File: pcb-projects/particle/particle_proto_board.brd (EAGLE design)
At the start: 100 x 80 mm, 5 parts, among them IC1 ATTINY20-SOIC-14S1, IC2 DMC2400UV-SOT563, IC3 DMC2400UV-SOT563

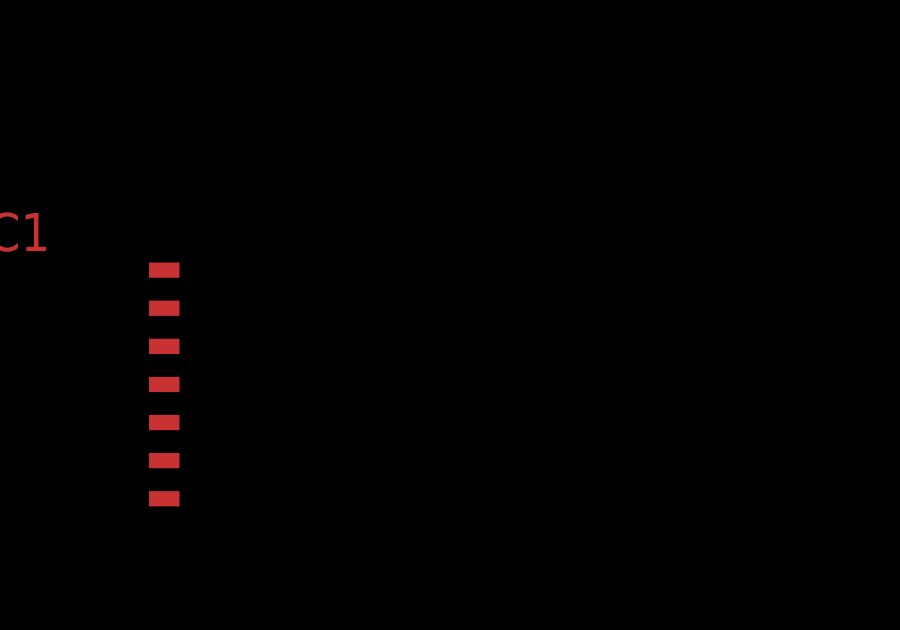
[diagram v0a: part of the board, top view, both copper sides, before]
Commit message: begun with tpi connector
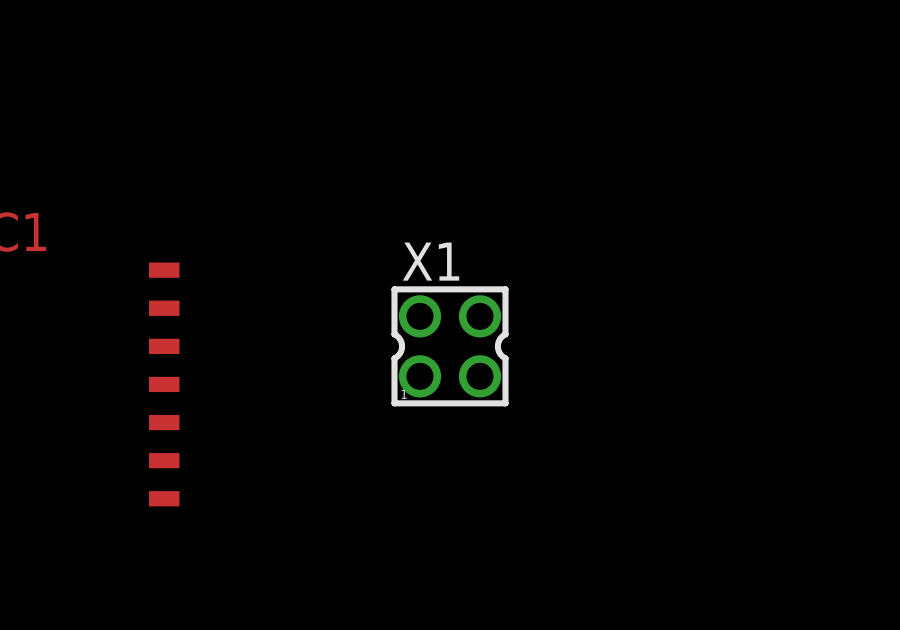
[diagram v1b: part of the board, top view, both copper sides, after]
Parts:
- added X1: 332-04, con-garry:332-04
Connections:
- net PWR_RX_B_SW renamed PWR_RX_SW_B
- new net N$4: IC1.11
- new net N$5: IC1.12
- new net N$6: IC1.13
- new net PWR_RX_SW_A: IC1.8, IC2.5
- new net RESET: IC1.3
- new net TPI_CLK: IC1.2
- net PWR_RX_A_SW: no longer IC2.5
- net PWR_TX_A: now also IC1.10; no longer IC1.2
- net RX_A: now also IC1.9; no longer IC1.3
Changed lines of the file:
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@@
 <?xml version="1.0" encoding="utf-8"?>
 <!DOCTYPE eagle SYSTEM "eagle.dtd">
-<eagle version="6.6.0">
+<eagle version="7.2.0">
 <drawing>
 <settings>
@@
 <pass name="Default">
 <param name="RoutingGrid" value="50mil"/>
+<param name="AutoGrid" value="1"/>
+<param name="Efforts" value="0"/>
+<param name="TopRouterVariant" value="1"/>
 <param name="tpViaShape" value="round"/>
 <param name="PrefDir.1" value="|"/>
@@
 <element name="R1" library="rcl" package="R1206" value="1k" x="27.94" y="34.29" rot="R180"/>
 <element name="R2" library="rcl" package="R1206" value="1k" x="27.94" y="26.67" rot="R180"/>
+<element name="X1" library="con-garry" package="332-04" value="332-04" x="60.96" y="30.48"/>
 </elements>
 <signals>
@@
 <wire x1="51.435" y1="33.02" x2="36.06" y2="32.32" width="0" layer="19" extent="1-1"/>
 </signal>
-<signal name="PWR_TX_A">
+<signal name="TPI_CLK">
 <contactref element="IC1" pad="2"/>
-<contactref element="IC2" pad="2"/>
-<wire x1="45.085" y1="31.75" x2="35.56" y2="33.72" width="0" layer="19" extent="1-1"/>
 </signal>
 <signal name="PWR_TX_B">
@@
 <wire x1="35.56" y1="27.37" x2="45.085" y2="27.94" width="0" layer="19" extent="1-1"/>
 </signal>
-<signal name="RX_A">
+<signal name="RESET">
 <contactref element="IC1" pad="3"/>
-<contactref element="IC2" pad="3"/>
-<wire x1="45.085" y1="30.48" x2="35.06" y2="33.72" width="0" layer="19" extent="1-1"/>
 </signal>
 <signal name="PWR_RX_A_SW">
 <contactref element="IC1" pad="4"/>
-<contactref element="IC2" pad="5"/>
-<wire x1="45.085" y1="29.21" x2="35.56" y2="32.32" width="0" layer="19" extent="1-1"/>
 </signal>
 <signal name="RX_B">
@@
 <wire x1="35.06" y1="27.37" x2="45.085" y2="26.67" width="0" layer="19" extent="1-1"/>
 </signal>
-<signal name="PWR_RX_B_SW">
+<signal name="PWR_RX_SW_B">
 <contactref element="IC1" pad="7"/>
 <contactref element="IC3" pad="5"/>
@@
 <wire x1="29.362" y1="26.67" x2="36.06" y2="27.37" width="0" layer="19" extent="1-1"/>
 </signal>
+<signal name="PWR_RX_SW_A">
+<contactref element="IC1" pad="8"/>
+<contactref element="IC2" pad="5"/>
+<wire x1="35.56" y1="32.32" x2="51.435" y2="25.4" width="0" layer="19" extent="1-1"/>
+</signal>
+<signal name="RX_A">
+<contactref element="IC1" pad="9"/>
+<contactref element="IC2" pad="3"/>
+<wire x1="35.06" y1="33.72" x2="51.435" y2="26.67" width="0" layer="19" extent="1-1"/>
+</signal>
+<signal name="PWR_TX_A">
+<contactref element="IC1" pad="10"/>
+<contactref element="IC2" pad="2"/>
+<wire x1="35.56" y1="33.72" x2="51.435" y2="27.94" width="0" layer="19" extent="1-1"/>
+</signal>
+<signal name="N$4">
+<contactref element="IC1" pad="11"/>
+</signal>
+<signal name="N$5">
+<contactref element="IC1" pad="12"/>
+</signal>
+<signal name="N$6">
+<contactref element="IC1" pad="13"/>
+</signal>
 </signals>

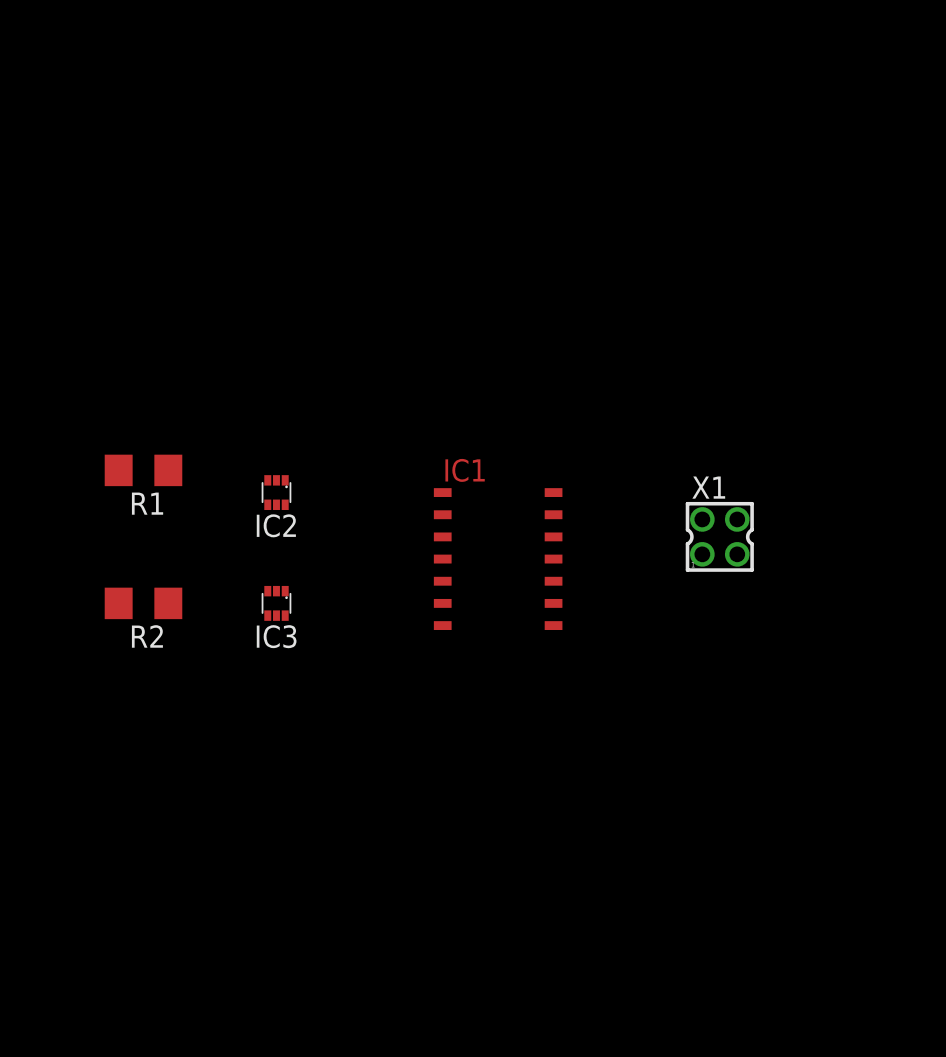
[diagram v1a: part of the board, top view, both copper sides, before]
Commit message: begun with routing
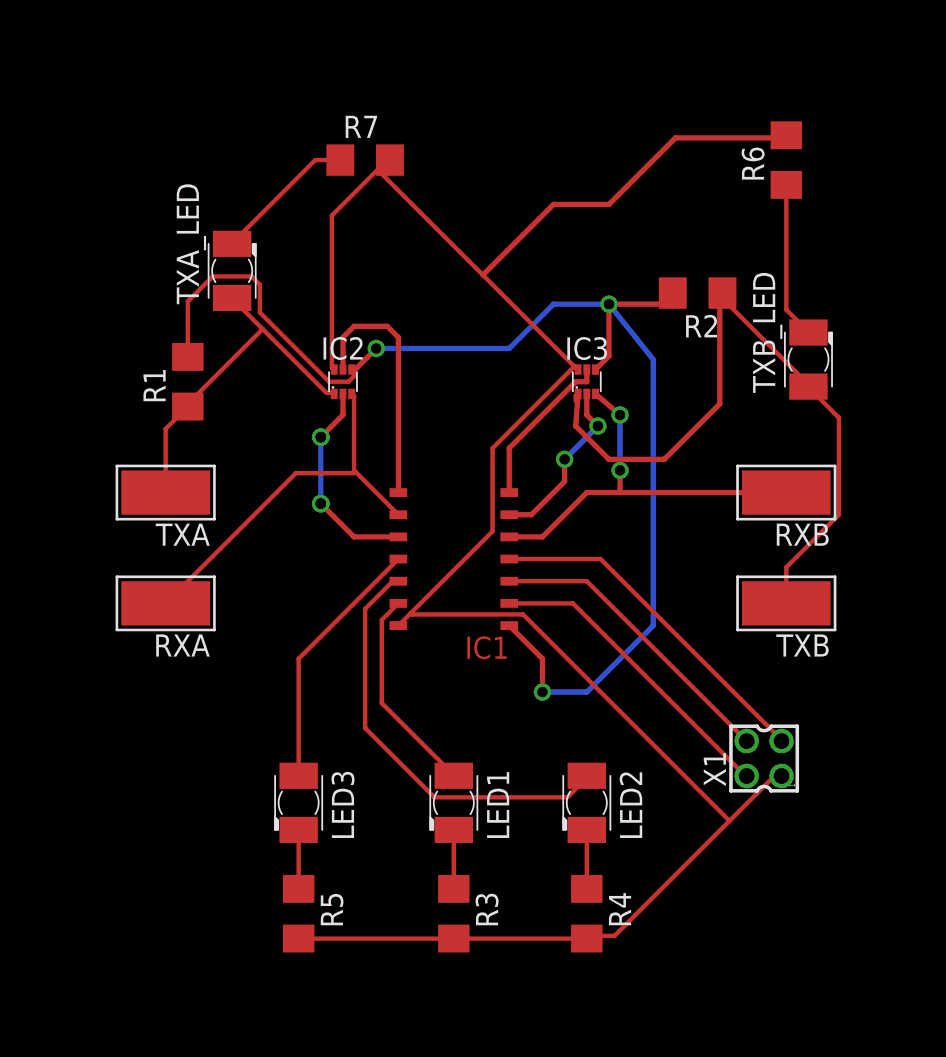
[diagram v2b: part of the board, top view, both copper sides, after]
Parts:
- added LED1, LED2, LED3, TXA_LED, TXB_LED: a, led:KA-3528ASYC
- added R3, R4, R5, R6, R7: 470, rcl:R1206
- added RXA, RXB, TXA, TXB: WIREPADSMD5-2,5, wirepad:5-2,5
- moved R2 36.4 mm to (59.7, 44.5)
- moved IC3 21.8 mm to (53.3, 39.4), turned to 0 degrees
- moved X1 13.0 mm to (63.5, 17.8), turned to 90 degrees
- moved IC2 7.41 mm to (39.4, 39.4), turned to 0 degrees
- moved R1 5.68 mm to (30.5, 39.4), turned to 90 degrees
- moved IC1 2.54 mm to (45.7, 29.2), turned to 180 degrees
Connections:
- removed net PWR_RX_A_SW: IC1.4
- removed net PWR_TX_A_A_A1: IC3.1, R2.1
- new net N$1: IC1.13, LED1.A
- new net N$2: IC1.11, LED3.A
- new net N$3: IC1.12, LED2.A
- new net N$7: R7.1, TXA_LED.C
- new net N$8: LED3.C, R5.1
- new net TPI_DATA: IC1.3, X1.4
- new net TXB: IC3.1, R2.1, TXB.1, TXB_LED.A
- net GND: now also R3.2, R4.2, R5.2, R6.2, R7.2, X1.1
- net N$4: now also LED1.C, R3.1; no longer IC1.11
- net N$5: now also R6.1, TXB_LED.C; no longer IC1.12
- net N$6: now also LED2.C, R4.1; no longer IC1.13
- net PWR_TX_A_A_A: now also TXA.1, TXA_LED.A
- net PWR_TX_B: now also IC1.6; no longer IC1.5
- net RESET: now also IC1.4, X1.3; no longer IC1.3
- net RX_A: now also RXA.1
- net RX_B: now also IC1.5, RXB.1; no longer IC1.6
- net TPI_CLK: now also X1.2
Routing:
- net GND: track 0.00 -> 125.2 mm
- net +5V: track 0.00 -> 73.4 mm, vias 0 -> 3
- net TXB: track 0.00 -> 41.1 mm
- net N$3: track 0.00 -> 24.3 mm
- net RX_B: track 0.00 -> 23.2 mm, vias 0 -> 2
- net RX_A: track 0.00 -> 22.0 mm
- net RESET: track 0.00 -> 20.0 mm
- net PWR_TX_A_A_A: track 0.00 -> 19.8 mm
- net TPI_CLK: track 0.00 -> 17.7 mm
- net TPI_DATA: track 0.00 -> 17.4 mm
- net N$2: track 0.00 -> 14.8 mm
- net PWR_RX_SW_A: track 0.00 -> 14.4 mm
- net PWR_TX_A: track 0.00 -> 12.0 mm, vias 0 -> 2
- net N$1: track 0.00 -> 12.0 mm
- net PWR_TX_B: track 0.00 -> 10.0 mm, vias 0 -> 2
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
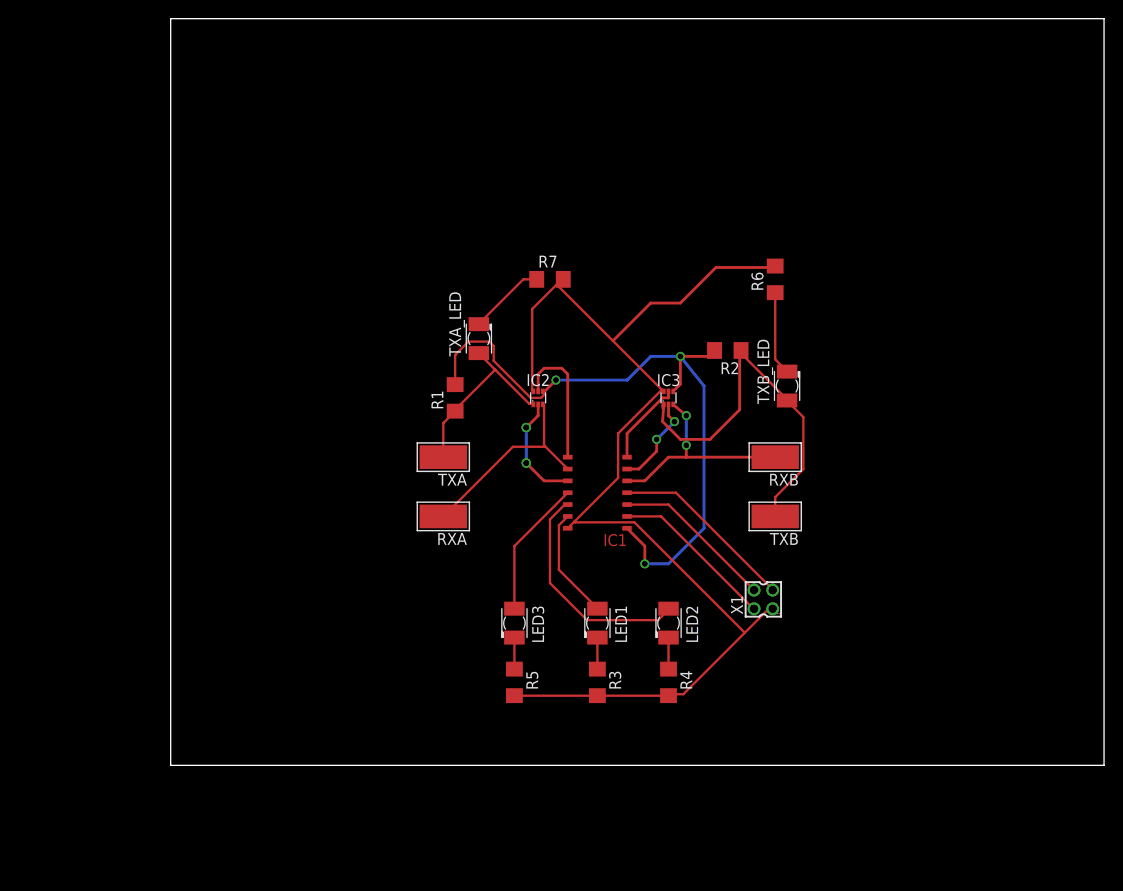
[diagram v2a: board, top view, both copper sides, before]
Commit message: added test pins
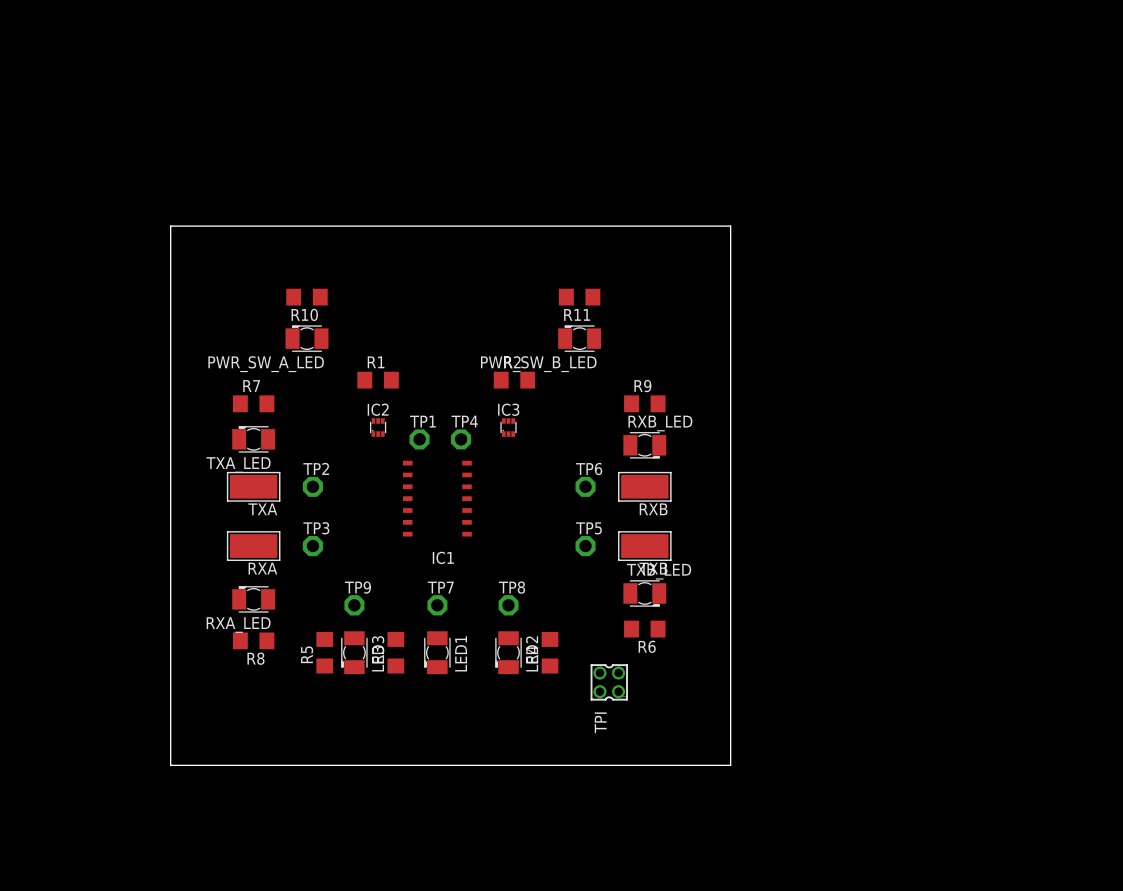
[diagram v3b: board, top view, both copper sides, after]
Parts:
- removed X1: 332-04, con-garry:332-04
- added PWR_SW_A_LED, PWR_SW_B_LED, RXA_LED, RXB_LED: a, led:KA-3528ASYC
- added R10, R11, R8, R9: 470, rcl:R1206
- added TP1, TP2, TP3, TP4, TP5, TP6, TP7, TP8, TP9: TPSPAD1-13, testpad:P1-13
- added TPI: 332-04, con-garry:332-04
- moved R6 40.0 mm to (50.8, 14.6), turned to 180 degrees
- moved R7 34.4 mm to (8.89, 38.7)
- moved TXB_LED 26.9 mm to (50.8, 18.4), turned to 0 degrees
- moved TXA_LED 26.4 mm to (8.89, 34.9), turned to 180 degrees
- moved R2 23.1 mm to (36.8, 41.3), turned to 0 degrees
- moved R3 21.8 mm to (24.1, 12.1), turned to 90 degrees
- moved RXA 20.6 mm to (8.89, 23.5)
- moved TXA 20.6 mm to (8.89, 29.8)
- moved R5 20.6 mm to (16.5, 12.1), turned to 90 degrees
- moved IC3 17.4 mm to (36.2, 36.2)
- moved LED2 17.4 mm to (36.2, 12.1)
- moved LED1 17.4 mm to (28.6, 12.1)
- moved LED3 17.4 mm to (19.7, 12.1)
- moved IC2 17.4 mm to (22.2, 36.2)
- moved IC1 17.2 mm to (28.6, 28.6), turned to 0 degrees
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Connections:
- new net N$11: R8.2, RXA_LED.C
- new net N$12: R9.2, RXB_LED.C
- new net N$13: PWR_SW_A_LED.C, R10.2
- new net N$14: PWR_SW_B_LED.C, R11.2
- net GND: now also R10.1, R11.1, R8.1, R9.1, TPI.1; no longer X1.1
- net N$1: now also TP7.TP
- net N$2: now also TP9.TP
- net N$3: now also TP8.TP
- net PWR_RX_SW_A: now also PWR_SW_A_LED.A, TP1.TP
- net PWR_RX_SW_B: now also PWR_SW_B_LED.A, TP4.TP
- net PWR_TX_A_A_A: now also TP2.TP
- net RESET: now also TPI.3; no longer X1.3
- net RX_A: now also RXA_LED.A, TP3.TP
- net RX_B: now also RXB_LED.A, TP6.TP
- net TPI_CLK: now also TPI.2; no longer X1.2
- net TPI_DATA: now also TPI.4; no longer X1.4
- net TXB: now also TP5.TP
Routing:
- net GND: track 125.2 -> 0.00 mm
- net +5V: track 73.4 -> 0.00 mm, vias 3 -> 0
- net TXB: track 41.1 -> 0.00 mm
- net N$3: track 24.3 -> 0.00 mm
- net RX_B: track 23.2 -> 0.00 mm, vias 2 -> 0
- net RX_A: track 22.0 -> 0.00 mm
- net RESET: track 20.0 -> 0.00 mm
- net PWR_TX_A_A_A: track 19.8 -> 0.00 mm
- net TPI_CLK: track 17.7 -> 0.00 mm
- net TPI_DATA: track 17.4 -> 0.00 mm
- net N$2: track 14.8 -> 0.00 mm
- net PWR_RX_SW_A: track 14.4 -> 0.00 mm
- net PWR_TX_A: track 12.0 -> 0.00 mm, vias 2 -> 0
- net N$1: track 12.0 -> 0.00 mm
- net PWR_TX_B: track 10.0 -> 0.00 mm, vias 2 -> 0
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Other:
- board size 100 x 80 mm -> 60 x 57.8 mm
